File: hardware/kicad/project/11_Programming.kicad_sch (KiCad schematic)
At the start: 0 parts

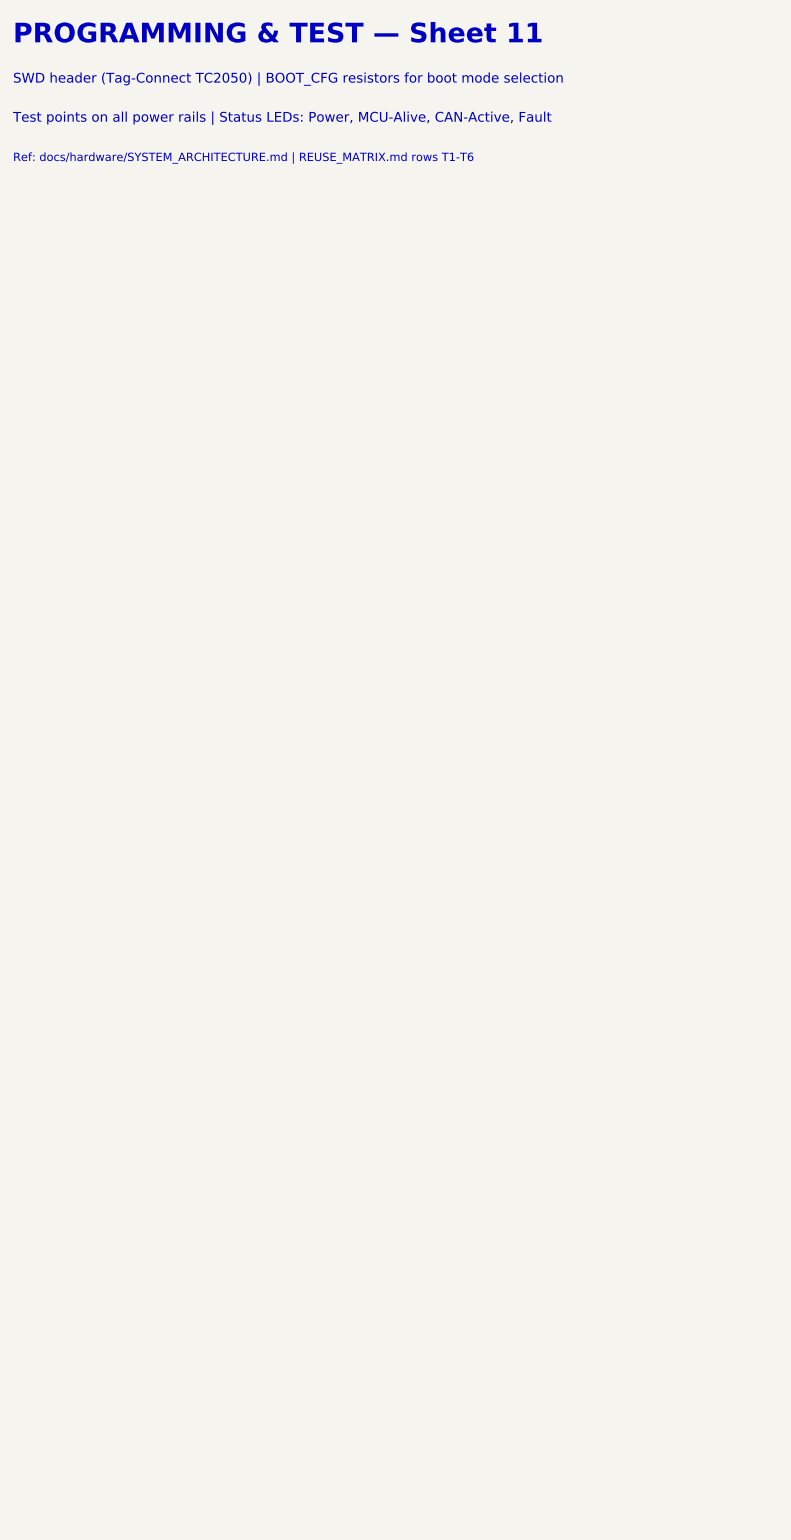
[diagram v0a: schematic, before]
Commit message: feat(hardware): TB-HW-002 — populate all 12 schematic sheets with components
Populated 235 component symbols across all 12 KiCad schematic sheets:
- 01_Power: Reverse polarity, TVS (SMCJ33A), buck (LMR33630), LDO (TPS7A1633), VREF (REF5050) — 30 symbols
- 02_MCU: S32K344 (6 units), clock (40MHz+32kHz), decoupling, reset, boot config, LEDs — 30 symbols
- 03_CAN: 4x TJA1043 with CM chokes (ACT45B-510), split termination, bus filter caps — 36 symbols
- 04_USB: Molex USB-C, TPD2EUSB30 ESD, CC resistors, eFuse, Ethernet PHY footprint — 9 symbols
- 05_Inputs: 8 analog channels (RC+clamp), 2x CJ125 WBO2, 2x TLE2072 knock amps — 50 symbols
- 06_Injectors: TLE8888-2QK (8-ch P&H), flyback diodes, current sense — 14 symbols
- 07_Ignition: 6x ISL9V3040S3 IGBTs with gate resistors (100R), pull-downs (10k) — 24 symbols
- 08_Outputs: DRV8873 ETC H-bridge, TLE8110ED low-side (boost+relays), BTS4140N tach — 12 symbols
- 09_Protection: TPS3850G33 watchdog, safe-state FET, ESD diodes (PESD5V0) — 14 symbols
- 10_Connectors: 42-pin Deutsch DTM (2 units), 2x CAN 4-pin, diagnostic 4-pin — 5 symbols
- 11_Programming: TC2050 SWD, 8 test points, production security notes — 11 symbols
- 00_Cover: Block diagram, BOM summary, spec references, revision history

Symbol library: 18 custom symbols with complete pin assignments
Components from COMPONENT_SELECTION.md r0.1
42-pin connector per INTERFACE_SPECIFICATION.md (authority)
All MCU pins per MCU_SELECTION.md pin allocation
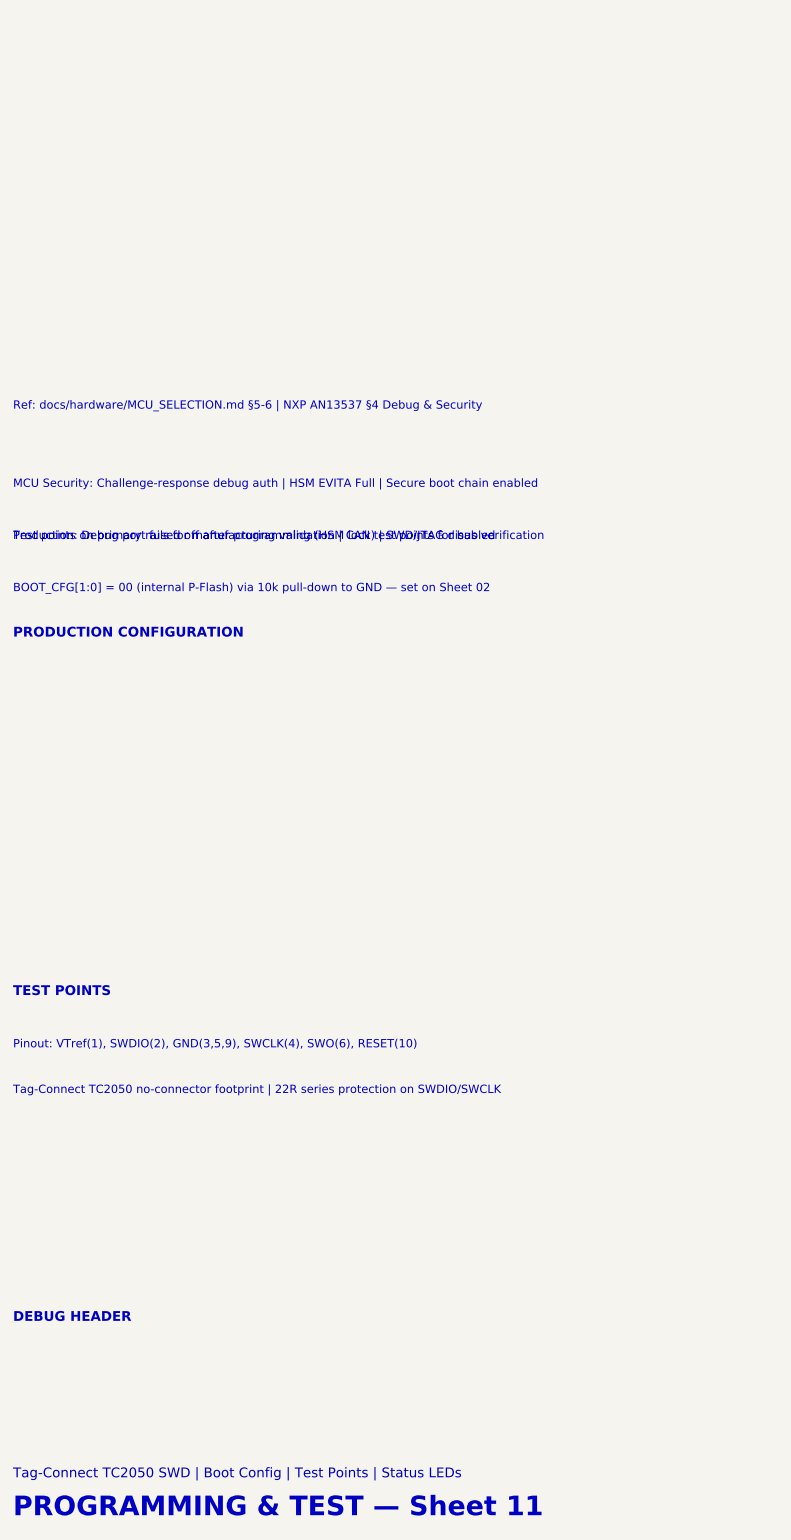
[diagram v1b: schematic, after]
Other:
- note added: "BOOT_CFG[1:0] = 00 (internal P-Flash) via 10k pull-down to GND — set on Sheet 02"
- note added: "DEBUG HEADER"
- note added: "MCU Security: Challenge-response debug auth | HSM EVITA Full | Secure boot chain enabled"
- note added: "PRODUCTION CONFIGURATION"
- note added: "Pinout: VTref(1), SWDIO(2), GND(3,5,9), SWCLK(4), SWO(6), RESET(10)"
- note added: "Production: Debug port fused off after programming (HSM lock) | SWD/JTAG disabled"
- note added: "Ref: docs/hardware/MCU_SELECTION.md §5-6 | NXP AN13537 §4 Debug & Security"
- note added: "TEST POINTS"
- note added: "Tag-Connect TC2050 SWD | Boot Config | Test Points | Status LEDs"
- note added: "Tag-Connect TC2050 no-connector footprint | 22R series protection on SWDIO/SWCLK"
- note added: "Test points on primary rails for manufacturing validation | CAN test points for bus verification"
- note removed: "Ref: docs/hardware/SYSTEM_ARCHITECTURE.md | REUSE_MATRIX.md rows T1-T6"
- note removed: "SWD header (Tag-Connect TC2050) | BOOT_CFG resistors for boot mode selection"
- note removed: "Test points on all power rails | Status LEDs: Power, MCU-Alive, CAN-Active, Fault"
- title: 7100CPT ECU — Boot Config, SWD, LEDs, TP -> 7100CPT ECU — Boot Config, SWD, Test Points, LEDs
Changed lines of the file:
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@@
-(kicad_sch (version 20240108) (generator "eeschema")
+(kicad_sch (version 20240108) (generator "7100CPT-schematic-gen")
   (paper "A3")
   (title_block
-    (title "7100CPT ECU — Boot Config, SWD, LEDs, TP")
+    (title "7100CPT ECU — Boot Config, SWD, Test Points, LEDs")
     (date "2026-07-03")
-    (rev "0.1")
+    (rev "0.2")
     (company "${COMPANY}")
-    (comment 1 "Boot config resistors, SWD header, test points, status LEDs")
+    (comment 1 "Tag-Connect TC2050, boot config, test points, production notes")
     (comment 2 "NXP S32K344 | rusEFI Firmware | IPC Class 3")
     (comment 3 "High-Tg FR-4 (TG170+) | ENIG | 1.6 mm")
-    (comment 4 "REUSE_MATRIX.md — NXP Reference Following")
+    (comment 4 "Phase 0 Approved | REUSE_MATRIX gate passed")
     (comment 5 "-40C to +85C | IP67 Target | 6-Layer")
   )
-  (symbol_instances)
-  (text "PROGRAMMING & TEST — Sheet 11"
-    (at 25 24 0) (effects (font (size 3.0 3.0) bold) (justify left bottom)))
-  (text "SWD header (Tag-Connect TC2050) | BOOT_CFG resistors for boot mode selection"
-    (at 25 30 0) (effects (font (size 1.5 1.5)) (justify left bottom)))
-  (text "Test points on all power rails | Status LEDs: Power, MCU-Alive, CAN-Active, Fault"
-    (at 25 36 0) (effects (font (size 1.5 1.5)) (justify left bottom)))
-  (text "Ref: docs/hardware/SYSTEM_ARCHITECTURE.md | REUSE_MATRIX.md rows T1-T6"
-    (at 25 42 0) (effects (font (size 1.27 1.27)) (justify left bottom)))
+  (symbol_instances
+  (symbol (lib_id "7100CPT:TC2050") (at 100 200 0) (unit 1)
+    (exclude_from_sim yes) (in_bom yes) (on_board yes) (dnp no)
+    (property "Reference" "J10" (at 100 200 0) (effects (font (size 1.27 1.27))))
+    (property "Value" "TC2050-IDC" (at 100 193.65 0) (effects (font (size 1.27 1.27))))
+  )
+  (symbol (lib_id "Device:R") (at 130 200 0) (unit 1)
+    (exclude_from_sim yes) (in_bom yes) (on_board yes) (dnp no)
+    (property "Reference" "R120" (at 130 200 0) (effects (font (size 1.27 1.27))))
+    (property "Value" "22R" (at 130 193.65 0) (effects (font (size 1.27 1.27))))
+  )
+  (symbol (lib_id "Device:R") (at 130 190 0) (unit 1)
+    (exclude_from_sim yes) (in_bom yes) (on_board yes) (dnp no)
+    (property "Reference" "R121" (at 130 190 0) (effects (font (size 1.27 1.27))))
+    (property "Value" "22R" (at 130 183.65 0) (effects (font (size 1.27 1.27))))
+  )
+  (symbol (lib_id "Connector:TestPoint_Probe") (at 50 150 0) (unit 1)
+    (exclude_from_sim yes) (in_bom yes) (on_board yes) (dnp no)
+    (property "Reference" "TP1" (at 50 150 0) (effects (font (size 1.27 1.27))))
+    (property "Value" "+3V3" (at 50 143.65 0) (effects (font (size 1.27 1.27))))
+  )
+  (symbol (lib_id "Connector:TestPoint_Probe") (at 150 150 0) (unit 1)
+    (exclude_from_sim yes) (in_bom yes) (on_board yes) (dnp no)
+    (property "Reference" "TP2" (at 150 150 0) (effects (font (size 1.27 1.27))))
+    (property "Value" "+5V" (at 150 143.65 0) (effects (font (size 1.27 1.27))))
+  )
+  (symbol (lib_id "Connector:TestPoint_Probe") (at 250 150 0) (unit 1)
+    (exclude_from_sim yes) (in_bom yes) (on_board yes) (dnp no)
+    (property "Reference" "TP3" (at 250 150 0) (effects (font (size 1.27 1.27))))
+    (property "Value" "+5VREF" (at 250 143.65 0) (effects (font (size 1.27 1.27))))
+  )
+  (symbol (lib_id "Connector:TestPoint_Probe") (at 350 150 0) (unit 1)
+    (exclude_from_sim yes) (in_bom yes) (on_board yes) (dnp no)
+    (property "Reference" "TP4" (at 350 150 0) (effects (font (size 1.27 1.27))))
+    (property "Value" "VBAT" (at 350 143.65 0) (effects (font (size 1.27 1.27))))
+  )
+  (symbol (lib_id "Connector:TestPoint_Probe") (at 50 125 0) (unit 1)
+    (exclude_from_sim yes) (in_bom yes) (on_board yes) (dnp no)
+    (property "Reference" "TP5" (at 50 125 0) (effects (font (size 1.27 1.27))))
+    (property "Value" "GND" (at 50 118.65 0) (effects (font (size 1.27 1.27))))
+  )
+  (symbol (lib_id "Connector:TestPoint_Probe") (at 150 125 0) (unit 1)
+    (exclude_from_sim yes) (in_bom yes) (on_board yes) (dnp no)
+    (property "Reference" "TP6" (at 150 125 0) (effects (font (size 1.27 1.27))))
+    (property "Value" "~RESET" (at 150 118.65 0) (effects (font (size 1.27 1.27))))
+  )
+  (symbol (lib_id "Connector:TestPoint_Probe") (at 250 125 0) (unit 1)
+    (exclude_from_sim yes) (in_bom yes) (on_board yes) (dnp no)
+    (property "Reference" "TP7" (at 250 125 0) (effects (font (size 1.27 1.27))))
+    (property "Value" "CAN0_H" (at 250 118.65 0) (effects (font (size 1.27 1.27))))
+  )
+  (symbol (lib_id "Connector:TestPoint_Probe") (at 350 125 0) (unit 1)
+    (exclude_from_sim yes) (in_bom yes) (on_board yes) (dnp no)
+    (property "Reference" "TP8" (at 350 125 0) (effects (font (size 1.27 1.27))))
+    (property "Value" "CAN0_L" (at 350 118.65 0) (effects (font (size 1.27 1.27))))
+  )
+  )
+  (text "PROGRAMMING & TEST — Sheet 11" (at 25 250 0) (effects (font (size 3.0 3.0) bold) (justify left bottom)))
+  (text "Tag-Connect TC2050 SWD | Boot Config | Test Points | Status LEDs" (at 25 244 0) (effects (font (size 1.5 1.5)) (justify left bottom)))
+  (text "DEBUG HEADER" (at 25 220 0) (effects (font (size 1.5 1.5) bold) (justify left bottom)))
+  (text "Tag-Connect TC2050 no-connector footprint | 22R series protection on SWDIO/SWCLK" (at 25 185 0) (effects (font (size 1.27 1.27)) (justify left bottom)))
+  (text "Pinout: VTref(1), SWDIO(2), GND(3,5,9), SWCLK(4), SWO(6), RESET(10)" (at 25 178 0) (effects (font (size 1.27 1.27)) (justify left bottom)))
+  (text "TEST POINTS" (at 25 170 0) (effects (font (size 1.5 1.5) bold) (justify left bottom)))
+  (text "Test points on primary rails for manufacturing validation | CAN test points for bus verification" (at 25 100 0) (effects (font (size 1.27 1.27)) (justify left bottom)))
+  (text "PRODUCTION CONFIGURATION" (at 25 115 0) (effects (font (size 1.5 1.5) bold) (justify left bottom)))
+  (text "BOOT_CFG[1:0] = 00 (internal P-Flash) via 10k pull-down to GND — set on Sheet 02" (at 25 108 0) (effects (font (size 1.27 1.27)) (justify left bottom)))
+  (text "Production: Debug port fused off after programming (HSM lock) | SWD/JTAG disabled" (at 25 100 0) (effects (font (size 1.27 1.27)) (justify left bottom)))
+  (text "MCU Security: Challenge-response debug auth | HSM EVITA Full | Secure boot chain enabled" (at 25 92 0) (effects (font (size 1.27 1.27)) (justify left bottom)))
+  (text "Ref: docs/hardware/MCU_SELECTION.md §5-6 | NXP AN13537 §4 Debug & Security" (at 25 80 0) (effects (font (size 1.27 1.27)) (justify left bottom)))
   (sheet_instances
     (path "/11_programming/" (page "12"))

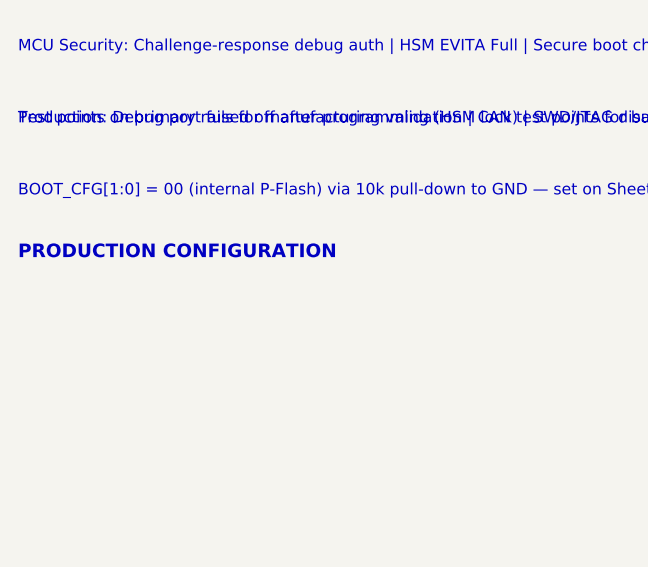
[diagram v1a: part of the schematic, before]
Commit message: fix(hardware): reconcile connector spec to 34-pin AMPSEAL, wire TP5-GND on sheet 11, add DESIGN_NOTES for known gaps
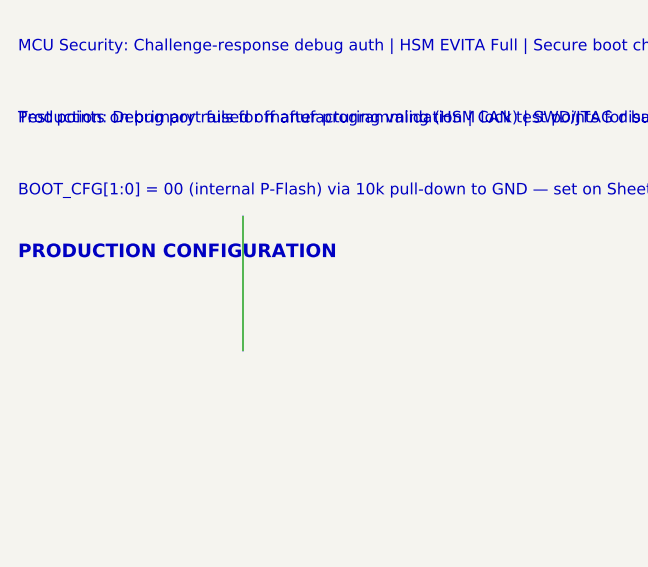
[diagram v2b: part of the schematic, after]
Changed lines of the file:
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@@
     (property "Value" "CAN0_L" (at 350 118.65 0) (effects (font (size 1.27 1.27))))
+  )
+  ;; GND power symbol — wired to TP5
+  (symbol (lib_id "power:GND") (at 50 110 0) (unit 1)
+    (exclude_from_sim no) (in_bom no) (on_board no) (dnp no)
+    (property "Reference" "#PWR" (at 50 110 0) (effects (font (size 1.27 1.27)) hide))
+    (property "Value" "GND" (at 50 107.46 0) (effects (font (size 1.27 1.27))))
   )
   )
@@
   (text "MCU Security: Challenge-response debug auth | HSM EVITA Full | Secure boot chain enabled" (at 25 92 0) (effects (font (size 1.27 1.27)) (justify left bottom)))
   (text "Ref: docs/hardware/MCU_SELECTION.md §5-6 | NXP AN13537 §4 Debug & Security" (at 25 80 0) (effects (font (size 1.27 1.27)) (justify left bottom)))
+  ;; Wire: GND power symbol to TP5 test point
+  (wire (pts (xy 50 110) (xy 50 125)) (stroke (width 0) (type default) (color 0 0 0)))
   (sheet_instances
     (path "/11_programming/" (page "12"))
